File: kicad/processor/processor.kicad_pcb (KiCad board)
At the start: 4 copper layers, 75 x 50 mm, 95 parts, among them J101 CONN_02X07, J201 V_QI, J202 GND, J203 Battery, M401 MICROSD, Q201 DMG3415U, Q202 DMG3415U, Q203 DMG3414U, Q204 DMG3415U, Q205 DMG3415U, Q301 DMG3415U, Q401 DMG3415U, Q501 MMBT4401, Q502 MMBT4401, SW201 SW, SW501 SWITCH_PUSHBUTTON, SW502 SWITCH_PUSHBUTTON, U101 ESP32-WROOM, U102 BME280, U103 TCA9534A, U201 MCP73832, U202 NCP694-3.3, U301 FGPMMOPA6H, U501 USB_B_Socket, U502 SP3003-04, U503 CP2102N

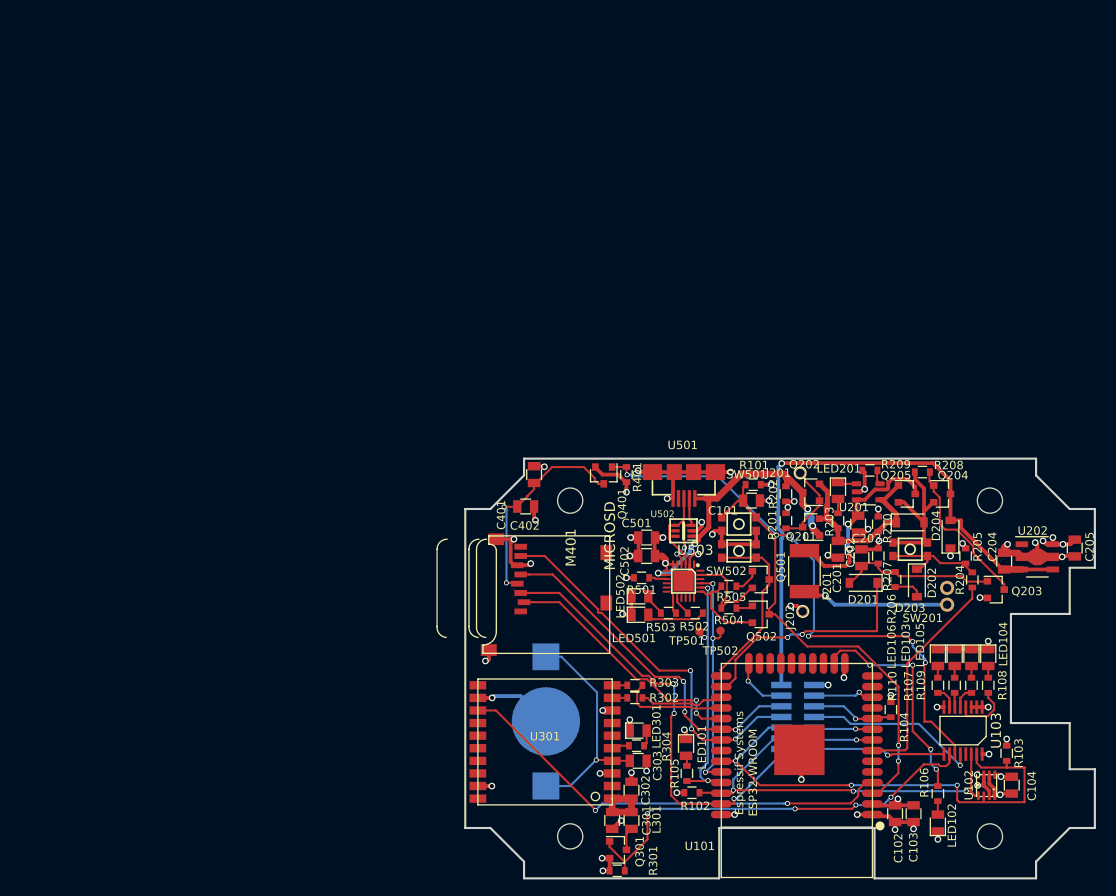
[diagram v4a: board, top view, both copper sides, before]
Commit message: Finished routing, DRC ok, moved origin to top left,
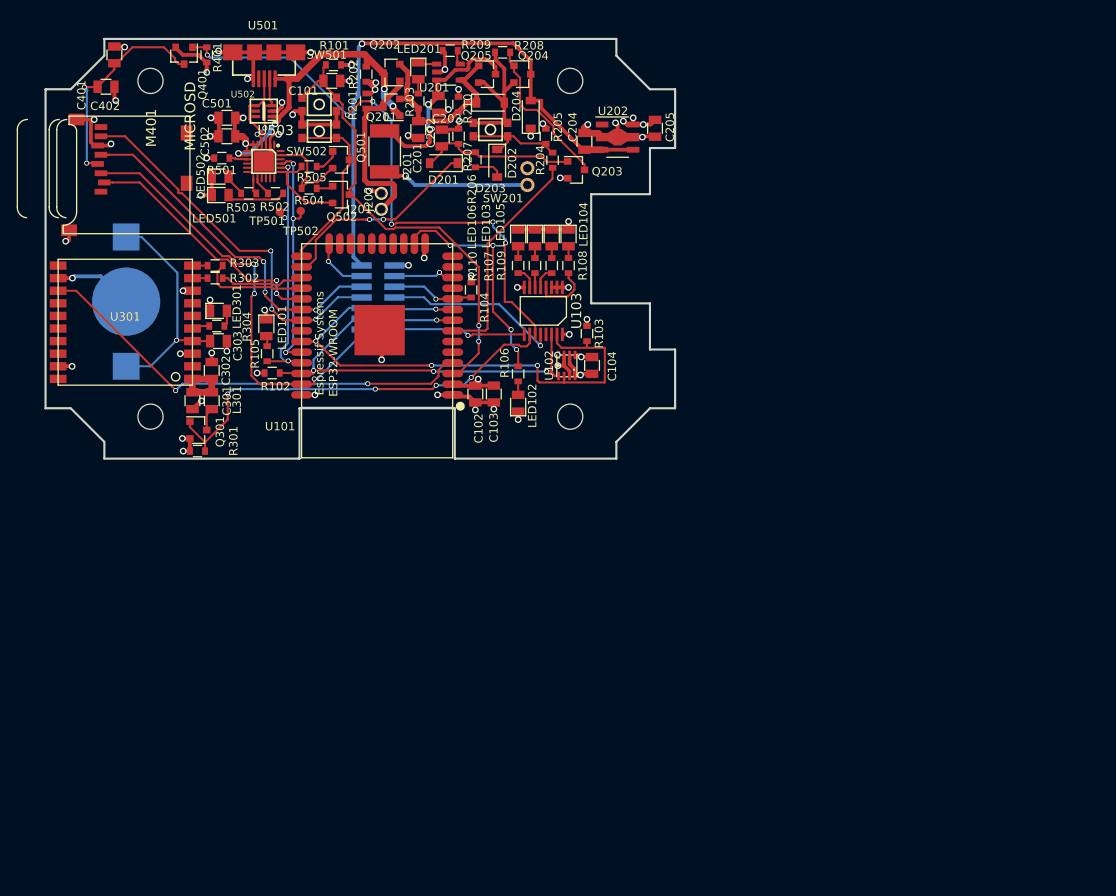
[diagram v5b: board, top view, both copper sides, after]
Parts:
- moved J202 70.7 mm to (40.0, 18.4)
- moved J203 70.7 mm to (57.4, 16.4)
- moved R502 70.7 mm to (27.4, 18.4)
- moved BT301 70.7 mm to (9.60, 31.3)
- moved C102 70.7 mm to (51.2, 42.3)
- moved C103 70.7 mm to (53.4, 42.3)
- moved C104 70.7 mm to (65.1, 38.9)
- moved C201 70.7 mm to (44.4, 10.8)
- moved C202 70.7 mm to (47.2, 11.8)
- moved C203 70.7 mm to (46.8, 7.80)
- moved C204 70.7 mm to (64.2, 12.2)
- moved C205 70.7 mm to (72.6, 10.7)
- moved C302 70.7 mm to (19.8, 39.5)
- moved C401 70.7 mm to (8.20, 1.90)
- moved C402 70.7 mm to (7.20, 5.70)
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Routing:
- net Net-(J201-Pad1): track 11.1 -> 22.0 mm
- net /KEEPALIVE: track 28.4 -> 25.1 mm
- net /SD_ENABLE*: track 67.2 -> 69.8 mm
- net GND: track 132.1 -> 133.5 mm
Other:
- rule via_min_size: 0.4 -> 0.6

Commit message: processor RC1
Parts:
- moved C401 3.98 mm to (7.00, 5.70), turned to 0 degrees
- moved C402 2.11 mm to (7.00, 7.80)
- moved Q401 0.50 mm to (17.0, 2.00)
- moved R401 0.30 mm to (19.5, 1.90)
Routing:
- net Net-(C401-Pad1): track 26.0 -> 28.0 mm
- net GND: track 133.5 -> 135.5 mm, vias 50 -> 49
- net Net-(BT301-Pad+): track 27.3 -> 26.1 mm
- net /I2C_SCK: track 48.5 -> 49.3 mm
- net /1PPS: track 53.7 -> 53.0 mm
- net +3V3: track 39.4 -> 39.9 mm
